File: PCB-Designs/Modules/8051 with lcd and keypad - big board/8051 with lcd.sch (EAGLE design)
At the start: 44 parts, among them IC1 AT89S51, IC2 7805TV

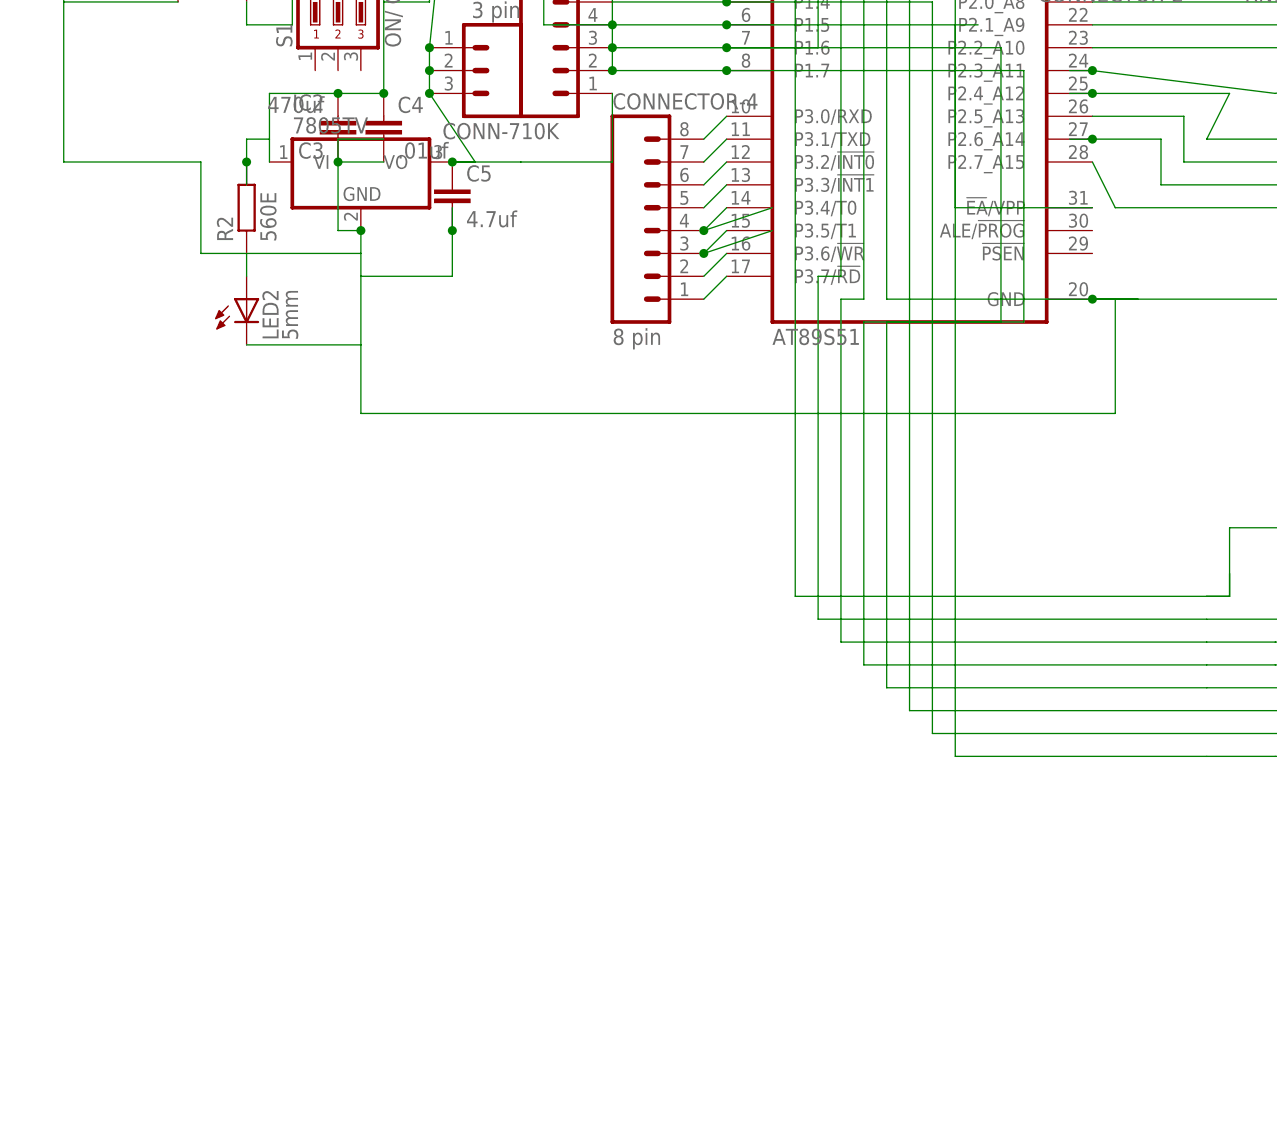
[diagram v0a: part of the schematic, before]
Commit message: 
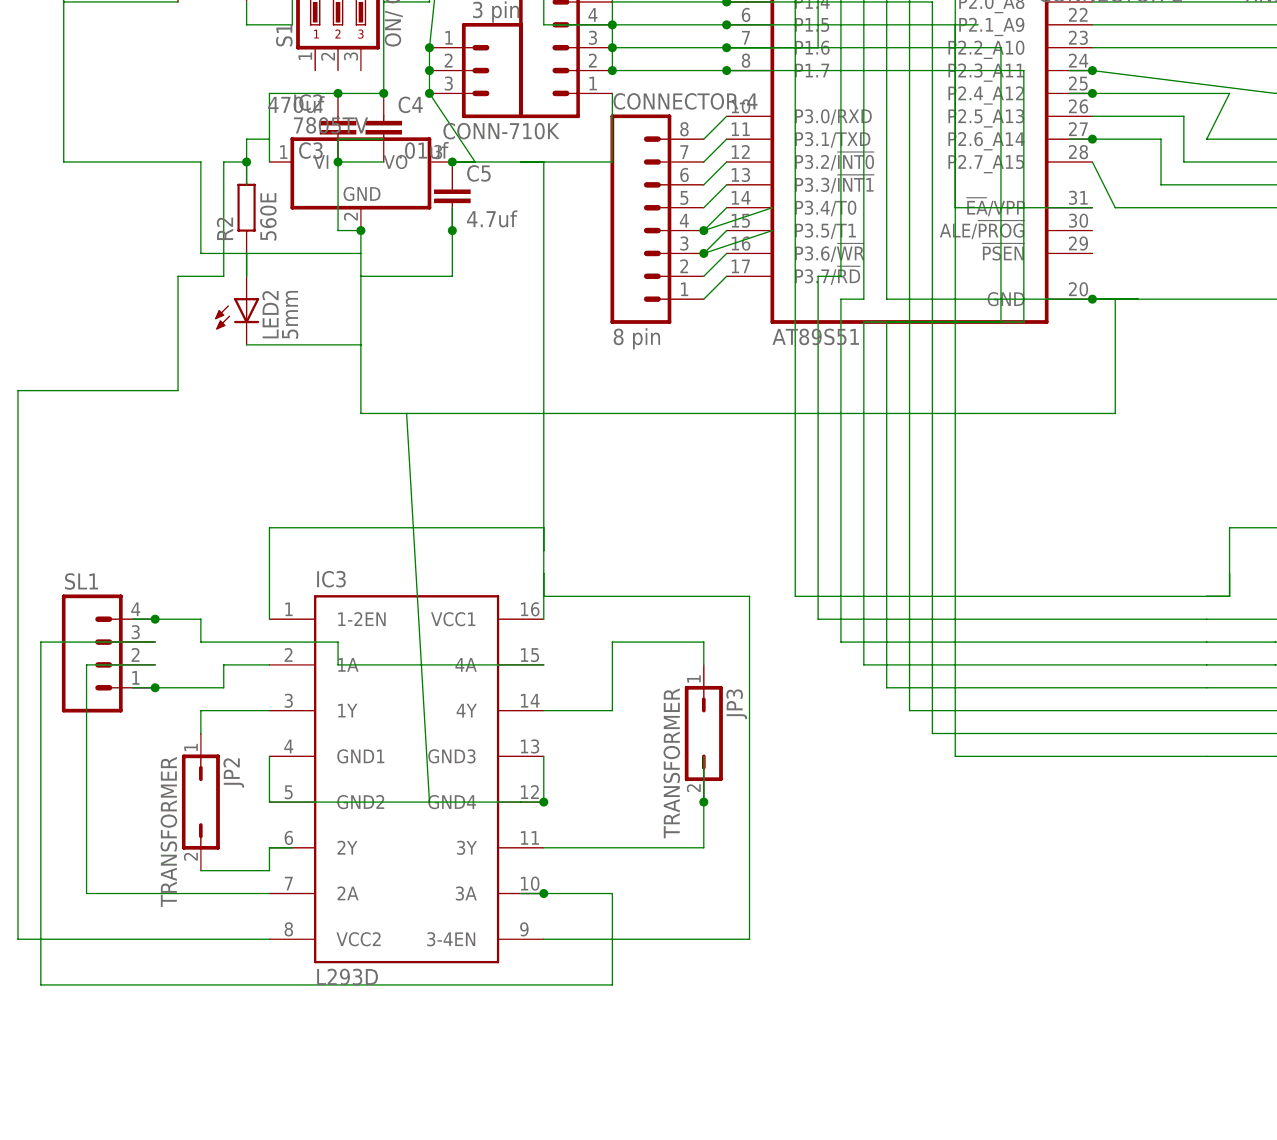
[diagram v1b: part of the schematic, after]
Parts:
- added IC3: L293D, st-microelectronics:L293D
- added JP2, JP3: TRANSFORMER, jumper:JP1Q
- added SL1: (no value), con-amp-quick:M04
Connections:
- removed net N$4: C3.2, C4.1, CONN-6.1, CONN-6.2, CONN-6.3, CONNECTOR-5.3, IC2.VI, R2.2, S1.5
- new net N$43: C3.2, C4.1, CONN-6.1, CONN-6.2, CONN-6.3, CONNECTOR-5.3, IC2.VI, IC3.VCC2, R2.2, S1.5
- new net N$56: BRIDGE.1, C1.2, C2.2, C3.1, C4.2, C5.2, CONNECTOR-5.1, CONNECTOR-5.2, CONNECTOR.1, CONNECTOR.16, CONNECTOR.5, IC1.GND, IC2.GND, IC3.GND1, IC3.GND2, IC3.GND3, IC3.GND4, LED2.C, R1.2, SL8.1, VR.A
- new net N$57: IC3.1Y, JP2.1
- new net N$59: IC3.2Y, JP2.2
- new net N$60: IC3.4Y, JP3.1
- new net N$61: IC3.3Y, JP3.2
- new net N$66: IC3.2A, SL1.2
- new net N$67: IC3.3A, SL1.3
- new net N$68: IC3.4A, SL1.4
- net N$39: now also IC3.1-2EN, IC3.3-4EN, IC3.VCC1
- net N$41: now also IC3.1A, SL1.1; no longer BRIDGE.1, C1.2, C2.2, C3.1, C4.2, C5.2, CONNECTOR-5.1, CONNECTOR-5.2, CONNECTOR.1, CONNECTOR.16, CONNECTOR.5, IC1.GND, IC2.GND, LED2.C, R1.2, SL8.1, VR.A

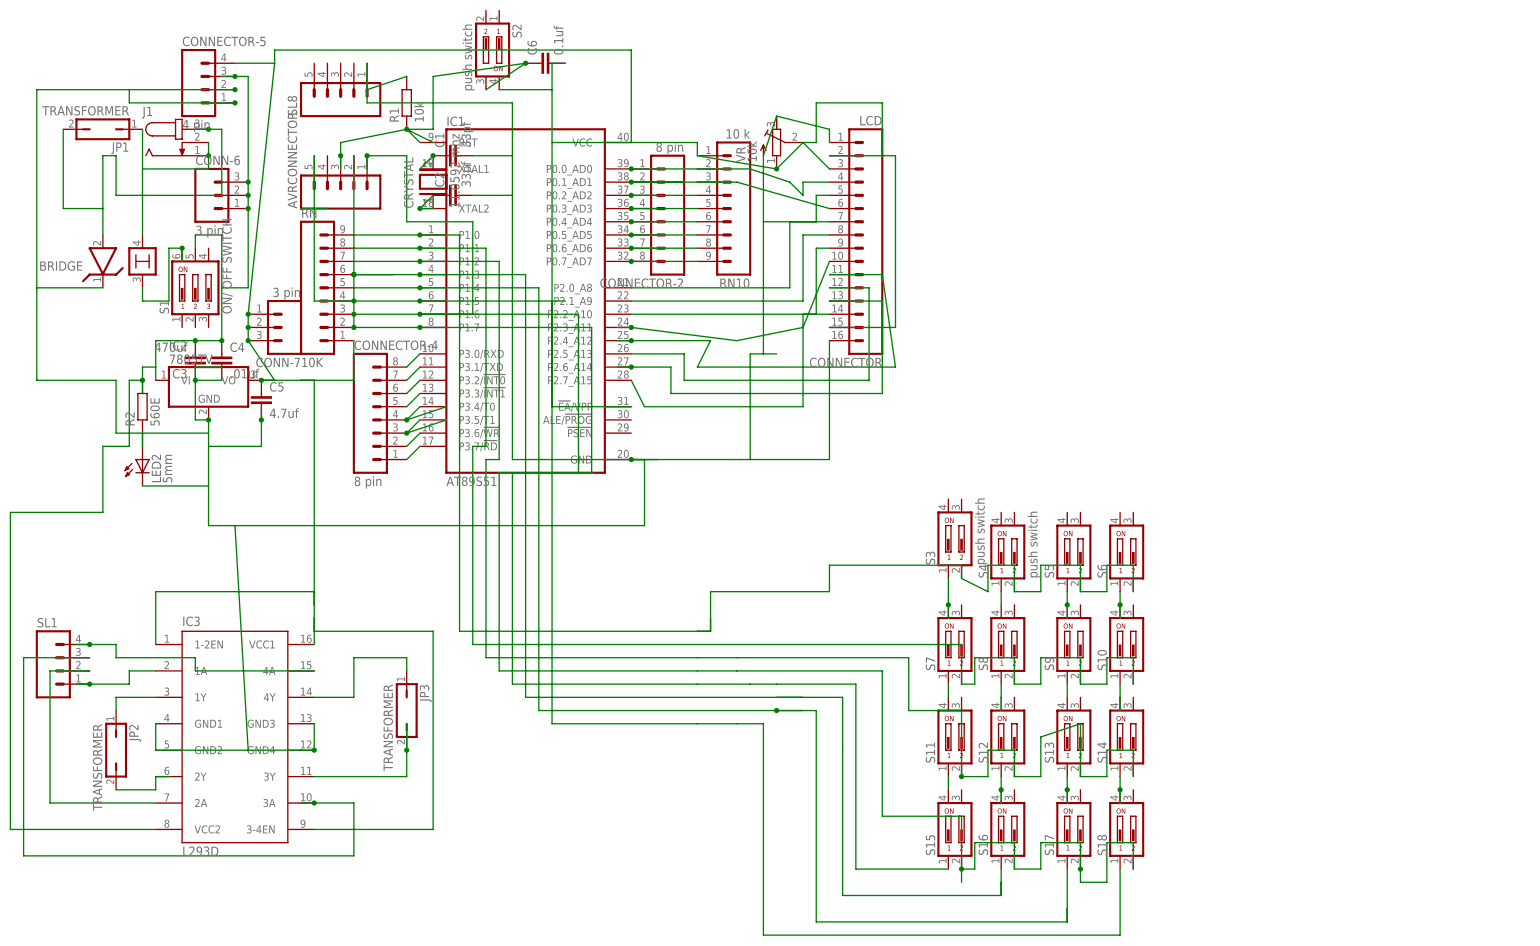
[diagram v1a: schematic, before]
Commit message: 
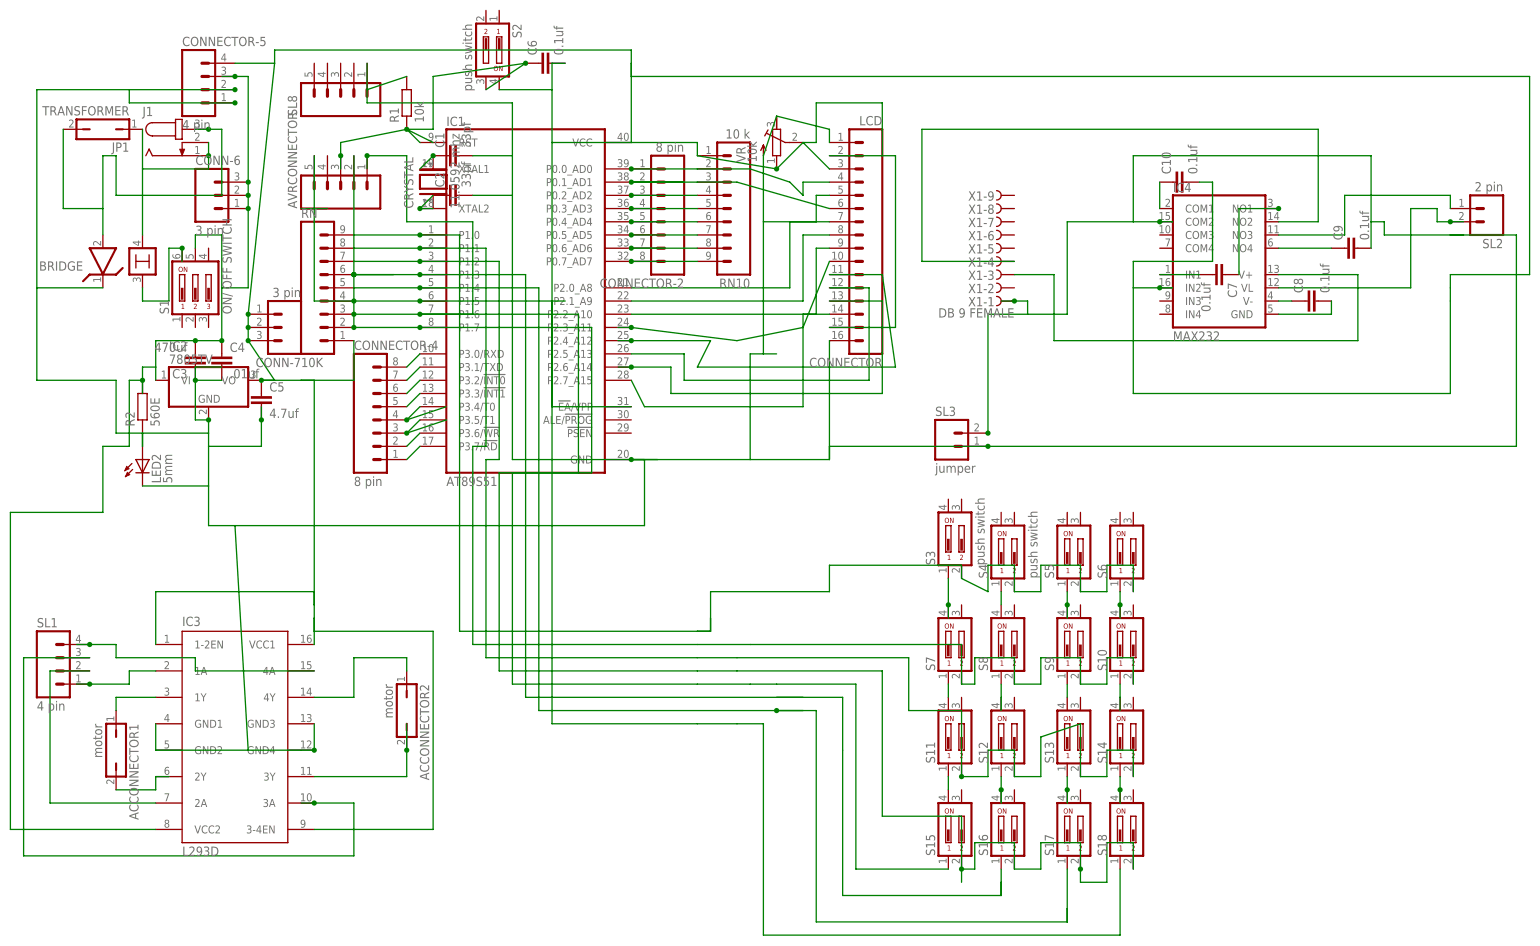
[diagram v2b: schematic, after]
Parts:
- added C10, C7, C8, C9: 0.1uf, capacitor-wima:C2,5-3
- added IC4: MAX232, maxim:MAX313EPE
- added SL2: 2 pin, con-amp-quick:M02
- added SL3: jumper, con-amp-quick:M02
- added X1: DB 9 FEMALE, con-thomas-betts:D-SUB9-H2M09ST
- ACCONNECTOR1, ACCONNECTOR2: value TRANSFORMER -> motor
- SL1: value (none) -> 4 pin
- renumbered JP2 to ACCONNECTOR1, JP3 to ACCONNECTOR2
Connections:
- removed net N$39: C5.1, C6.2, CONN-7.1, CONN-7.2, CONN-7.3, CONNECTOR-5.4, CONNECTOR.15, CONNECTOR.2, IC1.!EA!/VPP, IC1.VCC, IC2.VO, IC3.1-2EN, IC3.3-4EN, IC3.VCC1, RN.1, RN10.1, S2.4, VR.E
- removed net N$56: BRIDGE.1, C1.2, C2.2, C3.1, C4.2, C5.2, CONNECTOR-5.1, CONNECTOR-5.2, CONNECTOR.1, CONNECTOR.16, CONNECTOR.5, IC1.GND, IC2.GND, IC3.GND1, IC3.GND2, IC3.GND3, IC3.GND4, LED2.C, R1.2, SL8.1, VR.A
- new net N$23: C7.1, IC4.NO1
- new net N$4: C7.2, IC4.IN1
- new net N$53: C8.1, IC4.V-
- new net N$69: C8.2, IC4.GND
- new net N$70: C9.1, IC4.NO4
- new net N$72: BRIDGE.1, C1.2, C2.2, C3.1, C4.2, C5.2, C9.2, CONNECTOR-5.1, CONNECTOR-5.2, CONNECTOR.1, CONNECTOR.16, CONNECTOR.5, IC1.GND, IC2.GND, IC3.GND1, IC3.GND2, IC3.GND3, IC3.GND4, IC4.COM2, LED2.C, R1.2, SL3.1, SL3.2, SL8.1, VR.A, X1-1.F
- new net N$73: C10.1, IC4.COM1
- new net N$74: C10.2, C5.1, C6.2, CONN-7.1, CONN-7.2, CONN-7.3, CONNECTOR-5.4, CONNECTOR.15, CONNECTOR.2, IC1.!EA!/VPP, IC1.VCC, IC2.VO, IC3.1-2EN, IC3.3-4EN, IC3.VCC1, IC4.IN2, RN.1, RN10.1, S2.4, VR.E
- new net N$75: IC4.V+, X1-3.F
- new net N$76: IC4.NO2, X1-4.F
- new net N$77: IC4.NO3, SL2.1
- new net N$78: IC4.VL, SL2.2

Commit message: change
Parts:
- removed CONNECTOR-2, CONNECTOR-4: 8 pin, con-amp-quick:M08
- added SL4, SL5: (no value), con-amp-quick:M04
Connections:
- removed net N$10: CONNECTOR-4.4, IC1.P3.4/T0
- removed net N$11: CONNECTOR-4.3, IC1.P3.5/T1
- removed net N$12: CONNECTOR-4.2, IC1.P3.6/!WR
- removed net N$13: CONNECTOR-4.1, IC1.P3.7/!RD
- removed net N$22: S16.1
- removed net N$62: S4.1, S8.4
- net N$15: now also S4.1, S8.4
- net N$21: now also S3.2, S4.2, S5.2, S6.2
- net N$24: no longer CONNECTOR-2.3
- net N$25: no longer CONNECTOR-2.4
- net N$26: now also SL4.1; no longer CONNECTOR-2.5
- net N$27: now also SL4.2; no longer CONNECTOR-2.6
- net N$28: now also SL4.3; no longer CONNECTOR-2.7
- net N$29: now also SL4.4; no longer CONNECTOR-2.8
- net N$3: now also C9.2, IC4.COM2, SL3.2, X1-1.F; no longer S3.2, S4.2, S5.2, S6.2
- net N$48: no longer CONNECTOR-2.2
- net N$58: no longer CONNECTOR-2.1
- net N$6: now also IC1.P3.7/!RD, SL5.1; no longer CONNECTOR-4.8, IC1.P3.0/RXD
- net N$7: now also IC1.P3.6/!WR, SL5.2; no longer CONNECTOR-4.7, IC1.P3.1/TXD
- net N$72: no longer C9.2, IC4.COM2, SL3.2, X1-1.F
- net N$8: now also IC1.P3.5/T1, SL5.3; no longer CONNECTOR-4.6, IC1.P3.2/!INT0
- net N$9: now also IC1.P3.4/T0, SL5.4; no longer CONNECTOR-4.5, IC1.P3.3/!INT1
